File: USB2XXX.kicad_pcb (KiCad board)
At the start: 2 copper layers, 55.9 x 30.1 mm, 65 parts, among them J1 Conn_01x04, J2 Conn_01x03, J3 Conn_01x03, J4 Conn_01x02, J5 Conn_01x02, J6 Conn_01x04, J7 Conn_01x04, Q1 S8050, U1 STM32F072C8Tx, U2 TJA1051T-3, U3 HX9193, U4 STM32F072C8Tx, U5 TJA1051T-3, U6 SL2.1S, U7 CH340E, U8 CH340E, Y1 12M

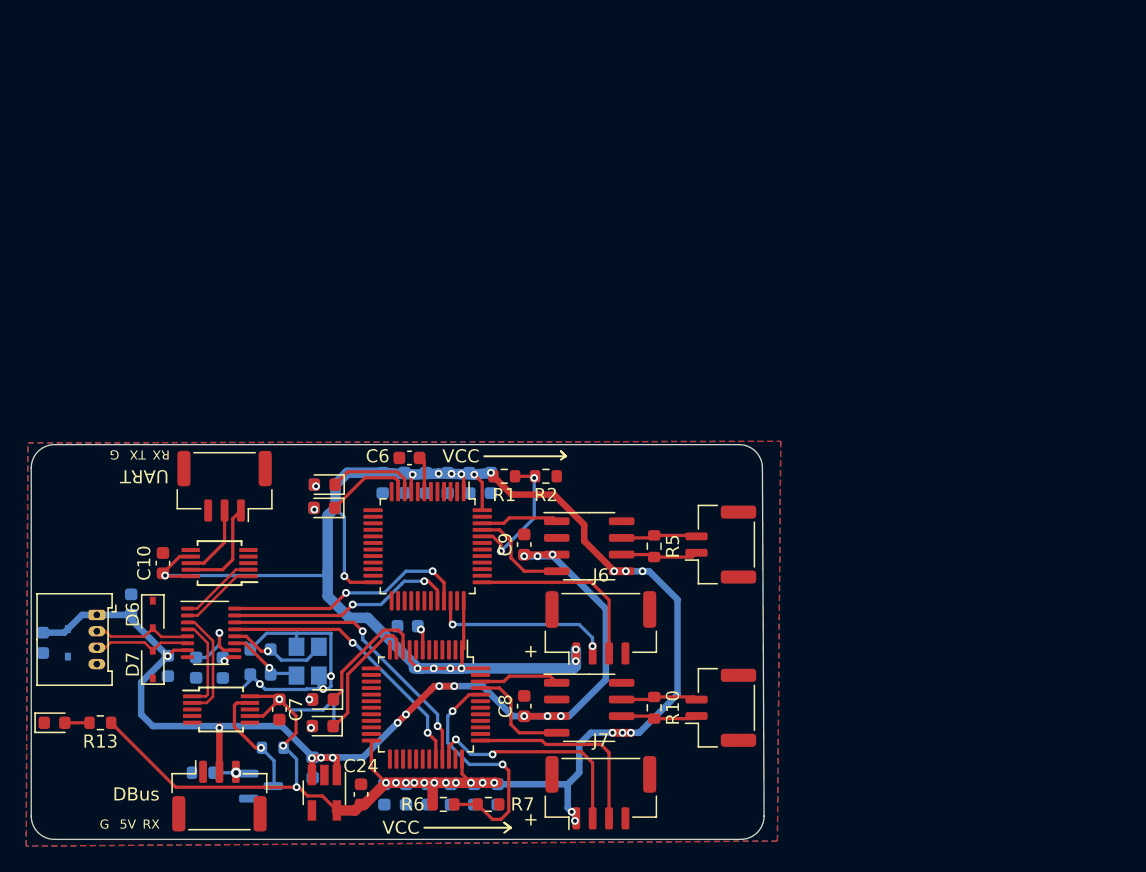
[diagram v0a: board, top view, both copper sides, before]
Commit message: New PCB design and single panel to SMT
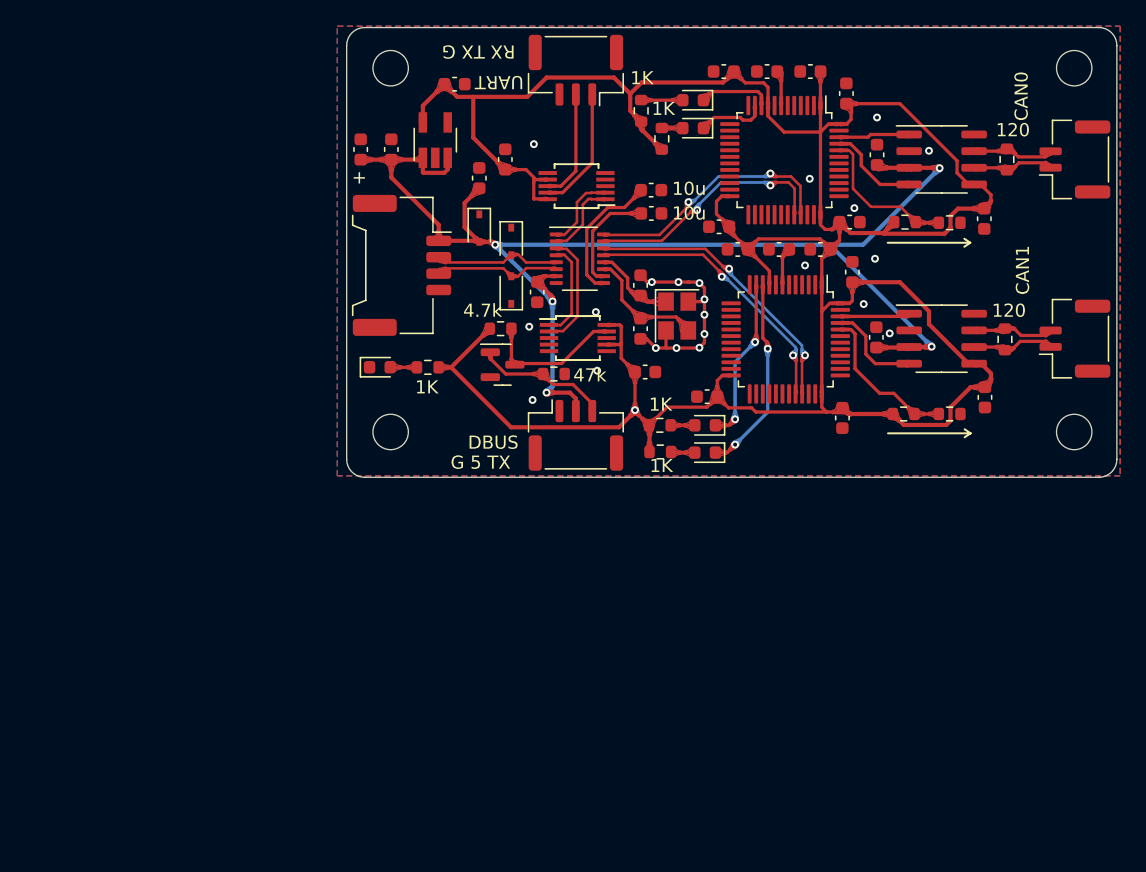
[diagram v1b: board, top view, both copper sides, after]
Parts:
- removed J6, J7: Conn_01x04, Connector_JST:JST_GH_BM04B-GHS-TBT_1x04-1MP_P1.25mm_Vertical
- added REF**: MountingHole_2.7mm_M2.5, MountingHole:MountingHole_2.7mm_M2.5, F.Cu at (141.1, 87.4)
- added REF**: MountingHole_2.7mm_M2.5, MountingHole:MountingHole_2.7mm_M2.5, F.Cu at (141.1, 59.7)
- added REF**: MountingHole_2.7mm_M2.5, MountingHole:MountingHole_2.7mm_M2.5, F.Cu at (89.0, 87.4)
- added REF**: MountingHole_2.7mm_M2.5, MountingHole:MountingHole_2.7mm_M2.5, F.Cu at (89.0, 59.7)
- C1, C11, C12, C13, C14, C15, C16, C17, C18, C19, C2, C20, C21, C22, C23, C25, C26, C27, C3, C4, C5, D5, Q1, R11, R12, R3, R4, R8, R9, Y1: moved to F.Cu
- J1: footprint Connector_Molex:Molex_PicoBlade_53048-0410_1x04_P1.25mm_Horizontal -> Connector_Molex:Molex_Panelmate_53780-0470_1x04-1MP_P1.25mm_Horizontal
- moved C23 73.7 mm to (126.1, 66.3), turned to 90 degrees
- moved C7 63.8 mm to (123.7, 61.6), turned to 90 degrees
- moved C27 59.6 mm to (126.0, 80.2), turned to 90 degrees
- moved C13 58.9 mm to (114.4, 59.9), turned to 180 degrees
- moved C10 55.5 mm to (121.8, 73.5), turned to 180 degrees
- moved C16 52.4 mm to (124.2, 75.2), turned to 90 degrees
- moved C12 52.2 mm to (124.0, 71.4), turned to 0 degrees
- moved C14 52.2 mm to (134.3, 84.8)
- moved C24 51.2 mm to (114.0, 71.8), turned to 180 degrees
- moved U3 50.5 mm to (92.4, 65.2), turned to 90 degrees
- moved C1 50.1 mm to (134.3, 71.2)
- moved C17 49.3 mm to (97.7, 66.6), turned to 90 degrees
- moved C20 49.0 mm to (108.9, 70.8), turned to 0 degrees
- moved C19 48.9 mm to (108.9, 69.0), turned to 0 degrees
- moved C26 47.5 mm to (89.1, 65.9), turned to 90 degrees
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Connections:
- net /STM1_CAN/USB_DM renamed /STM1_CAN/USB_D-
- net /STM1_CAN/USB_DP renamed /STM1_CAN/USB_D+
- net /STM2_CAN/USB_DM renamed /STM2_CAN/USB_D-
- net /STM2_CAN/USB_DP renamed /STM2_CAN/USB_D+
- Q1 pad 1: GND -> /DBUS/DBus
- Q1 pad 2: /DBUS/DBus -> GND
- U1 pad 34: /STM1_CAN/SWDIO -> unconnected-(U1-Pad34)
- U1 pad 37: /STM1_CAN/SWCLK -> unconnected-(U1-Pad37)
- U4 pad 34: /STM2_CAN/SWDIO -> unconnected-(U4-Pad34)
- U4 pad 37: /STM2_CAN/SWCLK -> unconnected-(U4-Pad37)
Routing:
- net VCC: track 198.0 -> 219.9 mm, vias 36 -> 1
- net /STM2_CAN/SWDIO: track 17.3 -> 0.00 mm, vias 2 -> 0
- net /STM2_CAN/SWCLK: track 15.2 -> 0.00 mm
- net +5V: track 88.2 -> 102.7 mm, vias 15 -> 5
- net /STM1_CAN/SWCLK: track 14.3 -> 0.00 mm
- net /STM1_CAN/SWDIO: track 13.6 -> 0.00 mm, vias 2 -> 0
- net Net-(C19-Pad1): track 0.91 -> 10.3 mm, vias 1 -> 0
- net /DBUS/DBus: track 2.71 -> 10.2 mm, vias 1 -> 0
- net Net-(R6-Pad1): track 18.7 -> 11.7 mm, vias 2 -> 0
- net /STM2_CAN/LED1: track 9.65 -> 15.1 mm, vias 0 -> 2
- net GND: track 22.2 -> 17.5 mm, vias 3 -> 22
- net /USB_HUB/XOUT: track 5.43 -> 9.42 mm, vias 1 -> 0
- net Net-(D1-Pad2): track 0.00 -> 3.18 mm, vias 1 -> 0
- net Net-(C20-Pad1): track 5.39 -> 8.35 mm, vias 1 -> 0
- net /UART/TXD: track 5.67 -> 8.31 mm
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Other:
- board size 55.9 x 30.1 mm -> 58.7 x 34.3 mm
- board text added: "10u"
- board text added: "120"
- board text added: "1K"
- board text added: "4.7k"
- board text added: "47k"
- board text added: "CAN0"
- board text added: "CAN1"
- board text added: "DBUS"
- board text added: "G 5 TX"
- board text added: "RX TX G"
- board text removed: "5V"
- board text removed: "DBus"
- board text removed: "G"
- board text removed: "RX"
- board text removed: "TX"
- board text removed: "VCC"

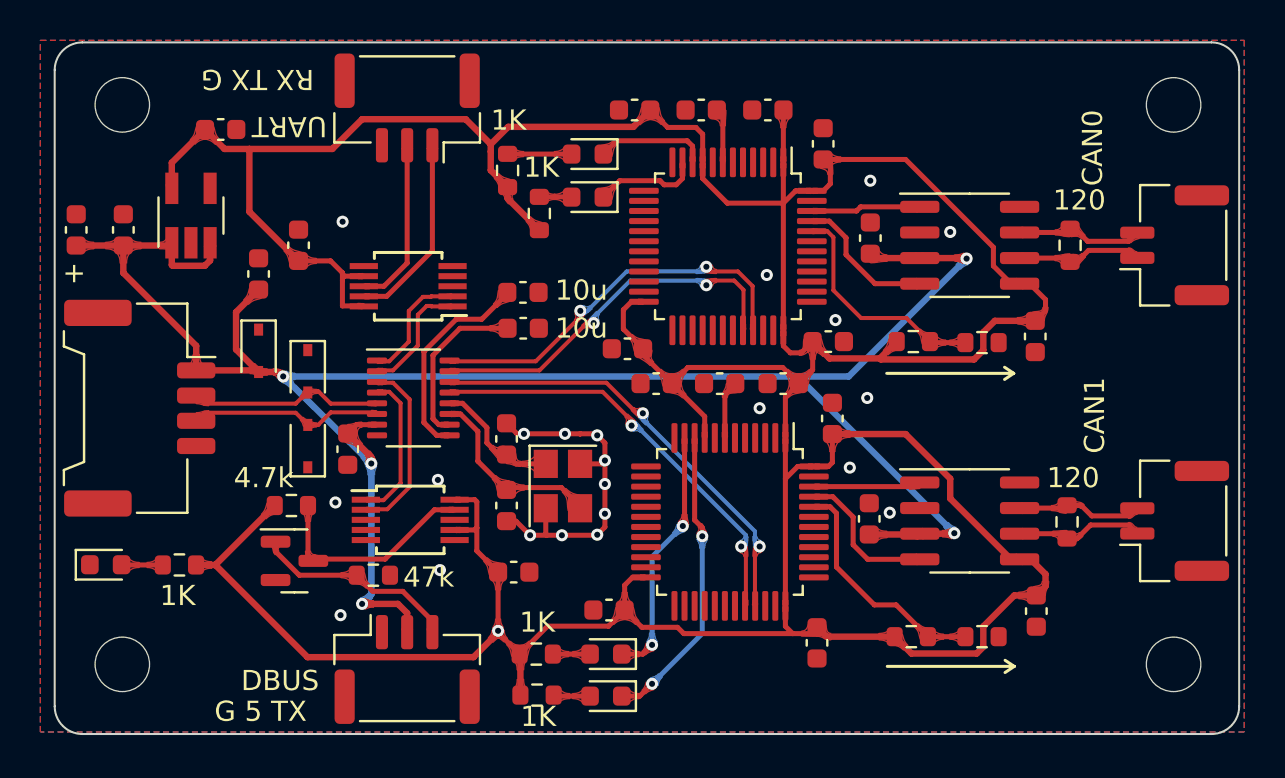
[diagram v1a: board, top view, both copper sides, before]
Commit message: update MX1.25 seat
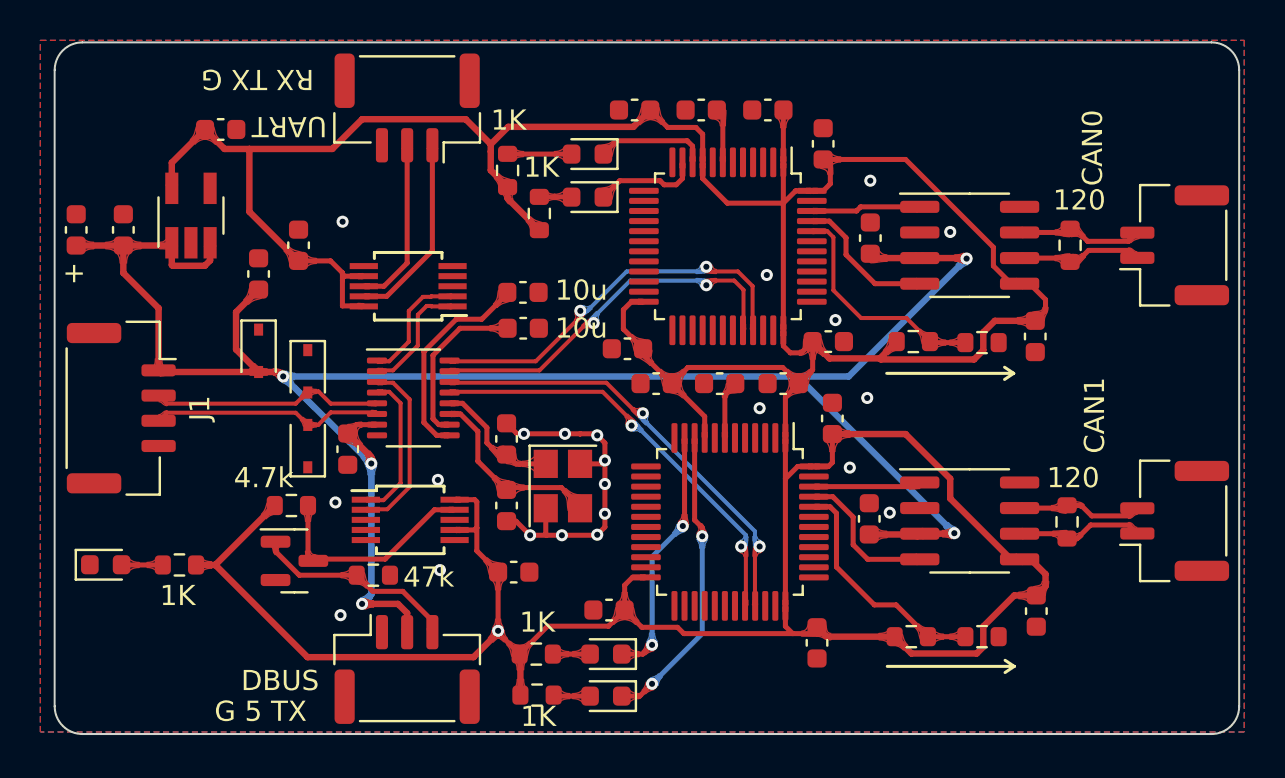
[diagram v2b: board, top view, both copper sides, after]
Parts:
- removed REF** (x4): MountingHole_2.7mm_M2.5, MountingHole:MountingHole_2.7mm_M2.5
- J1: footprint Connector_Molex:Molex_Panelmate_53780-0470_1x04-1MP_P1.25mm_Horizontal -> Connector_Molex:Molex_CLIK-Mate_502386-0470_1x04-1MP_P1.25mm_Horizontal
- moved J1 0.91 mm to (89.0, 74.7)
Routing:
- net /USB_HUB/D+: track 9.66 -> 11.5 mm
- net /USB_HUB/D-: track 9.69 -> 11.6 mm
- net +5V: track 102.7 -> 103.9 mm
